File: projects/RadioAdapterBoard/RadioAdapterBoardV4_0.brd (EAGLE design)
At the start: 20.2 x 45.5 mm, 5 parts

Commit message: Added LTC3112 to Radio Adaptor Board
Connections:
- removed net N$2: R1.1
- net GND: now also R1.1
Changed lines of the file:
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@@
 <vertex x="-23" y="-1.25"/>
 </polygon>
-<wire x1="-8.57" y1="24.79" x2="-8.57" y2="25.79" width="0" layer="19" extent="1-1"/>
-<wire x1="-8.57" y1="24.29" x2="-8.57" y2="24.79" width="0" layer="19" extent="1-1"/>
-<wire x1="-8.57" y1="23.79" x2="-8.57" y2="24.29" width="0" layer="19" extent="1-1"/>
-<wire x1="-8.57" y1="21.29" x2="-8.57" y2="23.79" width="0" layer="19" extent="1-1"/>
+<contactref element="R1" pad="1"/>
+<wire x1="-13.27" y1="18.79" x2="-35.4" y2="-24.5" width="0" layer="19" extent="1-1"/>
+<wire x1="-13.27" y1="20.79" x2="-13.27" y2="18.79" width="0" layer="19" extent="1-1"/>
+<wire x1="-13.27" y1="21.29" x2="-13.27" y2="20.79" width="0" layer="19" extent="1-1"/>
+<wire x1="-8.57" y1="21.29" x2="-13.27" y2="21.29" width="0" layer="19" extent="1-1"/>
 <wire x1="-8.57" y1="20.79" x2="-8.57" y2="21.29" width="0" layer="19" extent="1-1"/>
+<wire x1="-8.57" y1="23.79" x2="-8.57" y2="21.29" width="0" layer="19" extent="1-1"/>
+<wire x1="-8.57" y1="24.29" x2="-8.57" y2="23.79" width="0" layer="19" extent="1-1"/>
+<wire x1="-8.57" y1="24.79" x2="-8.57" y2="24.29" width="0" layer="19" extent="1-1"/>
+<wire x1="-8.57" y1="25.79" x2="-8.57" y2="24.79" width="0" layer="19" extent="1-1"/>
 <wire x1="-4.8752" y1="21.841" x2="-8.57" y2="21.29" width="0" layer="19" extent="1-1"/>
 <wire x1="-2.8752" y1="21.841" x2="-4.8752" y2="21.841" width="0" layer="19" extent="1-1"/>
-<wire x1="-13.27" y1="21.29" x2="-8.57" y2="21.29" width="0" layer="19" extent="1-1"/>
-<wire x1="-13.27" y1="20.79" x2="-13.27" y2="21.29" width="0" layer="19" extent="1-1"/>
-<wire x1="-13.27" y1="18.79" x2="-13.27" y2="20.79" width="0" layer="19" extent="1-1"/>
 </signal>
 <signal name="3V6">
@@
 <wire x1="-29.8625" y1="-20.4" x2="-33.6" y2="-28.75" width="0" layer="19" extent="1-1"/>
 </signal>
-<signal name="N$2">
-<contactref element="R1" pad="1"/>
-</signal>
 </signals>

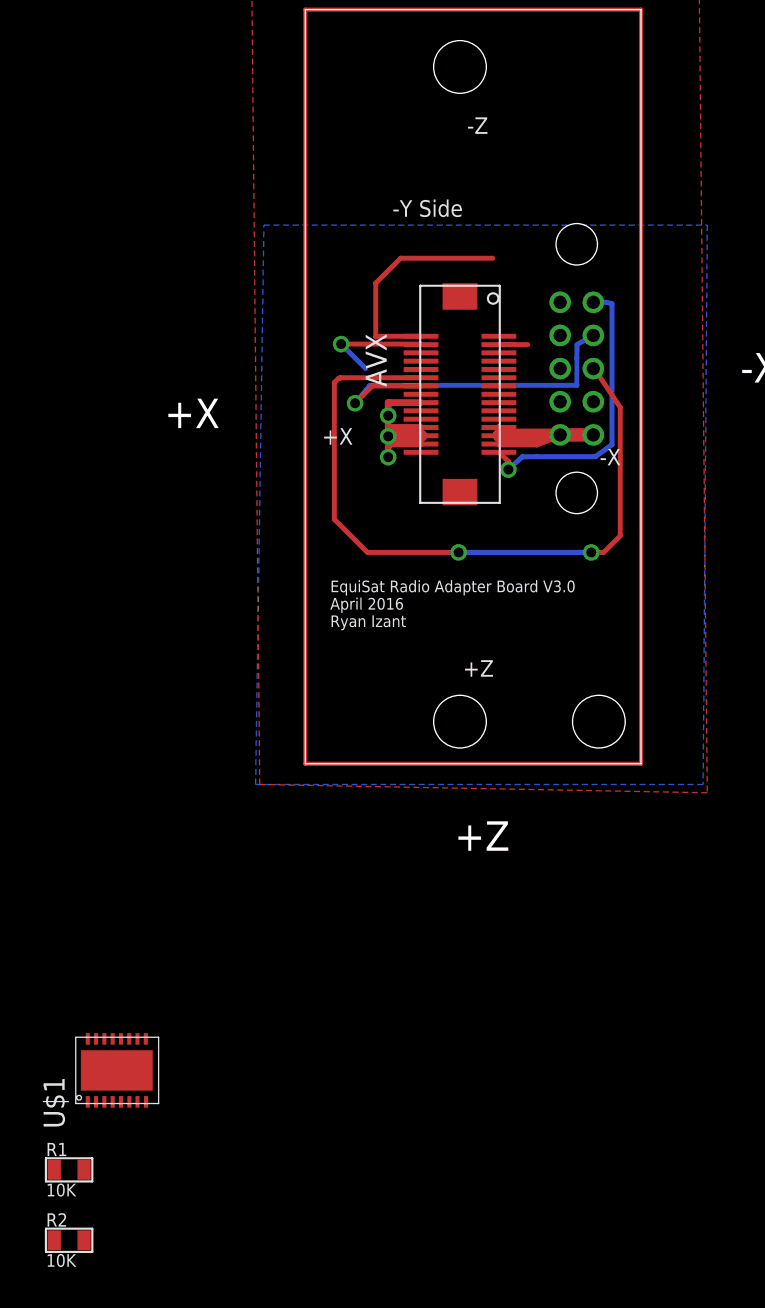
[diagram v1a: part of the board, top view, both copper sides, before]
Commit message: Changes to Radio Adapter Board V4
Moved LEDs to Radio Adapter Board
Flipped the connection to the radio so the radio is pointing into the
board
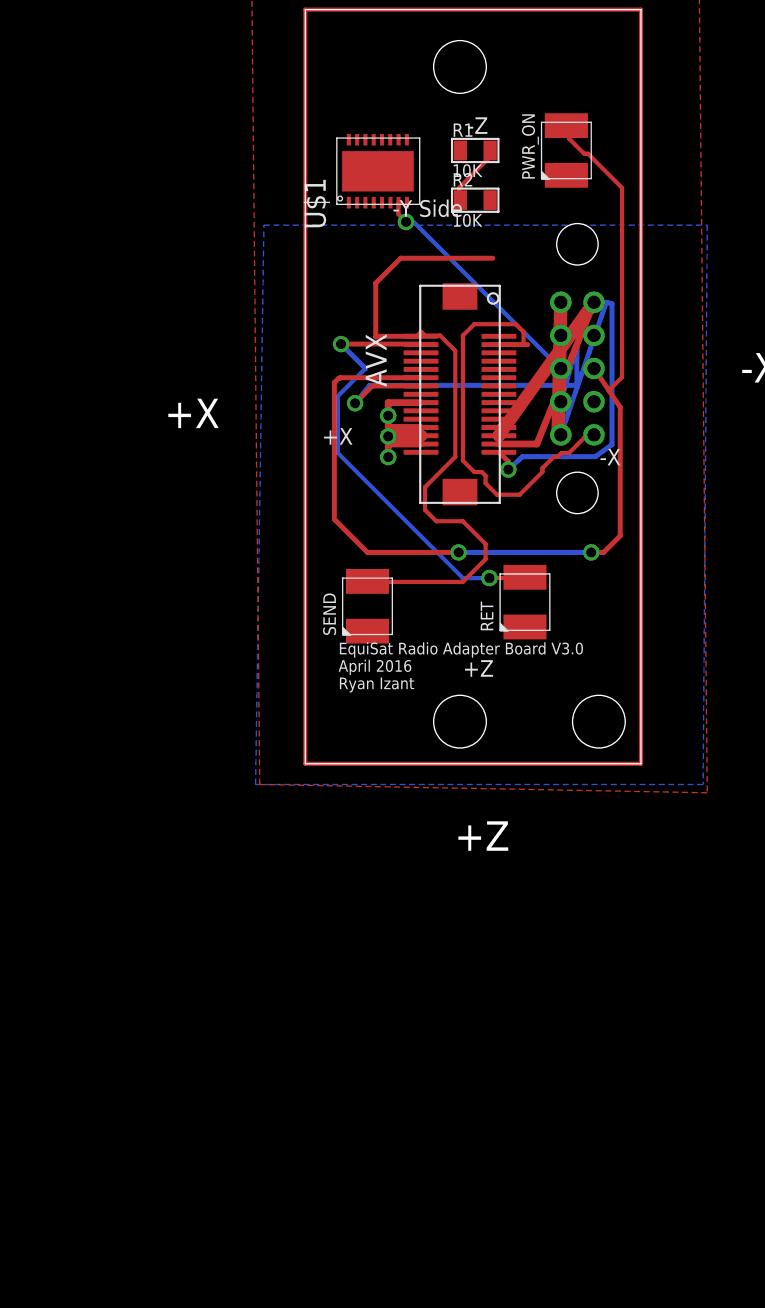
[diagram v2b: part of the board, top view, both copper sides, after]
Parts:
- added PWR_ON, RET, SEND: LT-T673-Q1R2-25-Z, CNTRL_BOARD:PLCC-2
- moved R2 67.4 mm to (-10.0, 34.0)
- moved R1 66.2 mm to (-10.0, 37.0)
- moved U$1 56.5 mm to (-17.8, 33.5)
- moved CNTRLCONN 8.25 mm to (-4.86, 27.8), turned to 270 degrees
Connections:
- net GND: now also PWR_ON.C, RET.C, SEND.C
- net P12: now also PWR_ON.A
- net P2: now also SEND.A
- net P4: now also RET.A
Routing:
- net P2: track 13.7 -> 40.2 mm
- net P3: track 1.74 -> 24.9 mm
- net P4: track 6.93 -> 27.2 mm, vias 1 -> 2
- net 3V6: track 20.4 -> 40.2 mm
- net P12: track 42.6 -> 60.4 mm
- net 3V6-SNS: track 0.00 -> 14.3 mm, vias 0 -> 1
- net P29: track 17.7 -> 25.4 mm
- net 3V6-REF: track 0.00 -> 3.96 mm
- net P14: track 21.9 -> 24.3 mm

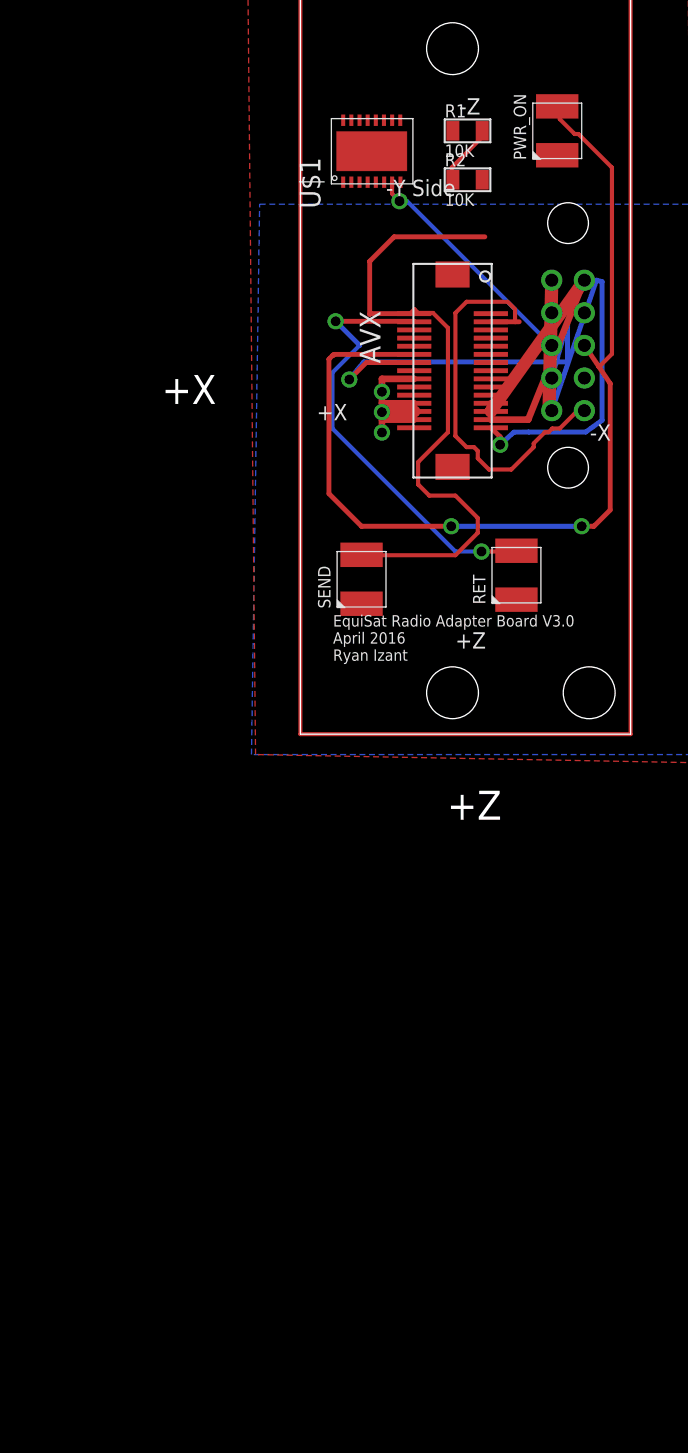
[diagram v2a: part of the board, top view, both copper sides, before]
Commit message: changes to Radio Adapter Board V4
Added the connections to LTC3112
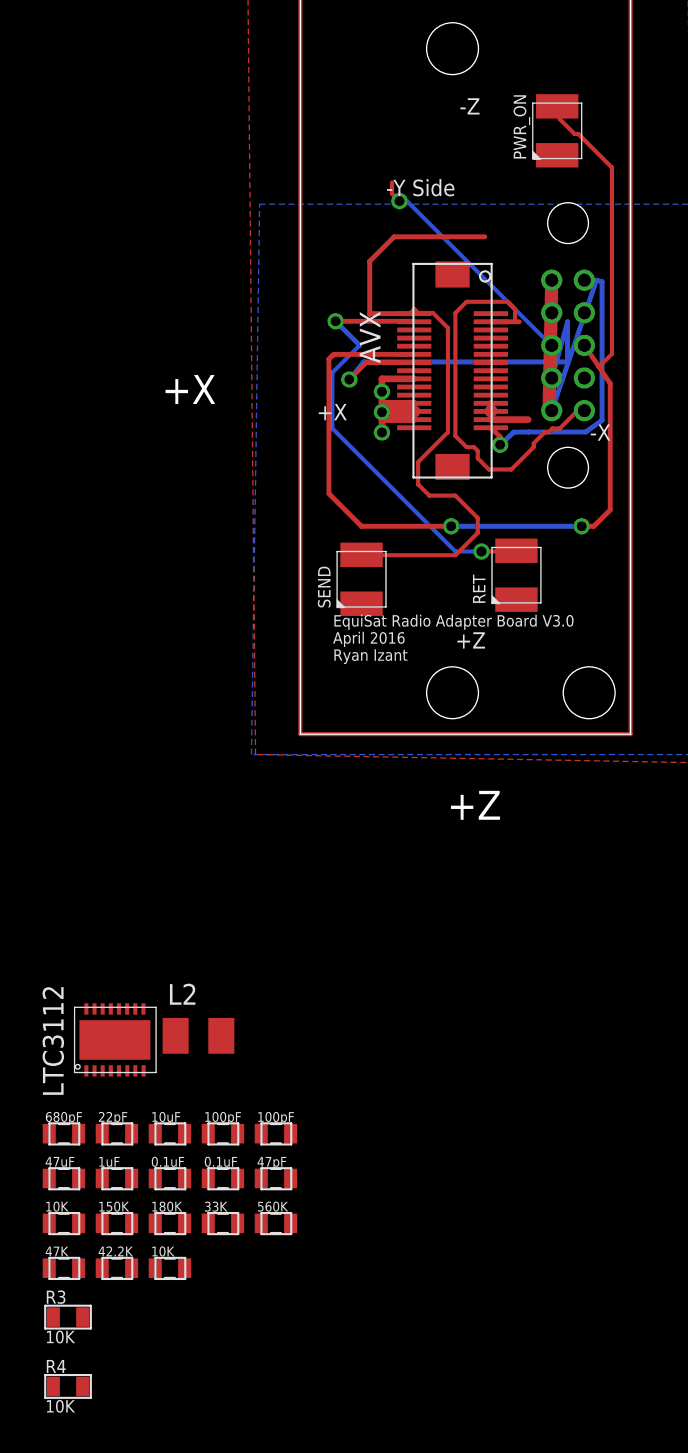
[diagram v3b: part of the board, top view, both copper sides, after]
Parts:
- removed R1, R2: 10K, BrownSpaceEngineering:0805
- removed U$1: (no value), CNTRL_BOARD:DHD16
- added C14: 680pF, CNTRL_BOARD:0805
- added C15: 22pF, CNTRL_BOARD:0805
- added C16: 10uF, CNTRL_BOARD:0805
- added C17, C18: 100pF, CNTRL_BOARD:0805
- added C19: 47uF, CNTRL_BOARD:0805
- added C20: 1uF, CNTRL_BOARD:0805
- added C21, C22: 0.1uF, CNTRL_BOARD:0805
- added C23: 47pF, CNTRL_BOARD:0805
- added L2: 4.7uH, resistor:L3225M
- added LTC3112: (no value), CNTRL_BOARD:DHD16
- added R10: 47K, CNTRL_BOARD:0805
- added R11: 42.2K, CNTRL_BOARD:0805
- added R12, R5: 10K, CNTRL_BOARD:0805
- added R3, R4: 10K, BrownSpaceEngineering:0805
- added R6: 150K, CNTRL_BOARD:0805
- added R7: 180K, CNTRL_BOARD:0805
- added R8: 33K, CNTRL_BOARD:0805
- added R9: 560K, CNTRL_BOARD:0805
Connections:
- removed net N$3: R2.2, U$1.8
- new net COMP: C14.2, C15.1, LTC3112.1
- new net FB: C15.2, LTC3112.2, R12.1, R6.1, R8.2, R9.2
- new net N$23: C20.2, LTC3112.15
- new net N$25: C22.1, LTC3112.14
- new net N$26: C22.2, L2.2, LTC3112.12, LTC3112.13
- new net N$28: C21.2, L2.1, LTC3112.10, LTC3112.9
- new net N$29: C21.1, LTC3112.11
- new net N$4: C14.1, R8.1
- new net N$5: C23.2, R12.2
- new net N$6: R5.1, R6.2
- new net OVP: C17.1, LTC3112.3, R10.2, R7.1
- new net VIN: C16.1, CNTRLCONN.P$1, CNTRLCONN.P$10, LTC3112.16, LTC3112.4, LTC3112.5
- net 3V6: now also C19.1, C23.1, LTC3112.8, R4.2, R7.2, R9.1; no longer CNTRLCONN.P$1, CNTRLCONN.P$10
- net 3V6-EN: now also LTC3112.6; no longer U$1.6
- net 3V6-REF: now also R3.2, R4.1; no longer R1.2, R2.1
- net 3V6-SNS: now also C18.1, LTC3112.7, R11.2; no longer U$1.7
- net GND: now also C16.2, C17.2, C18.2, C19.2, C20.1, LTC3112.17, R10.1, R11.1, R3.1, R5.2; no longer R1.1
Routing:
- net 3V6: track 40.2 -> 13.0 mm
- net VIN: track 0.00 -> 8.09 mm
- net 3V6-REF: track 3.96 -> 0.00 mm

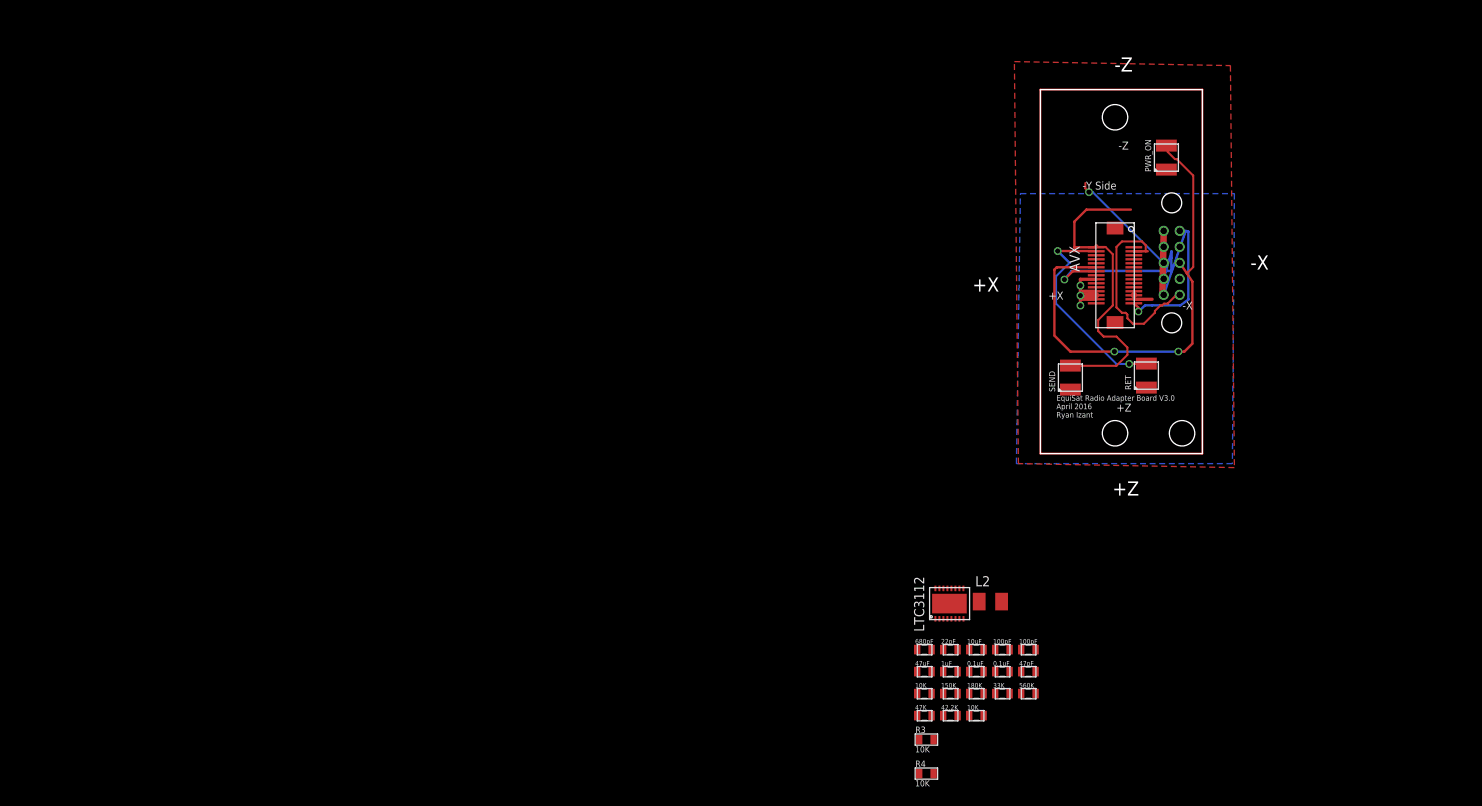
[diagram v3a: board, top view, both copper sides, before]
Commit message: Changes to Radio Adapter Board v4
In process of reordering physical components.
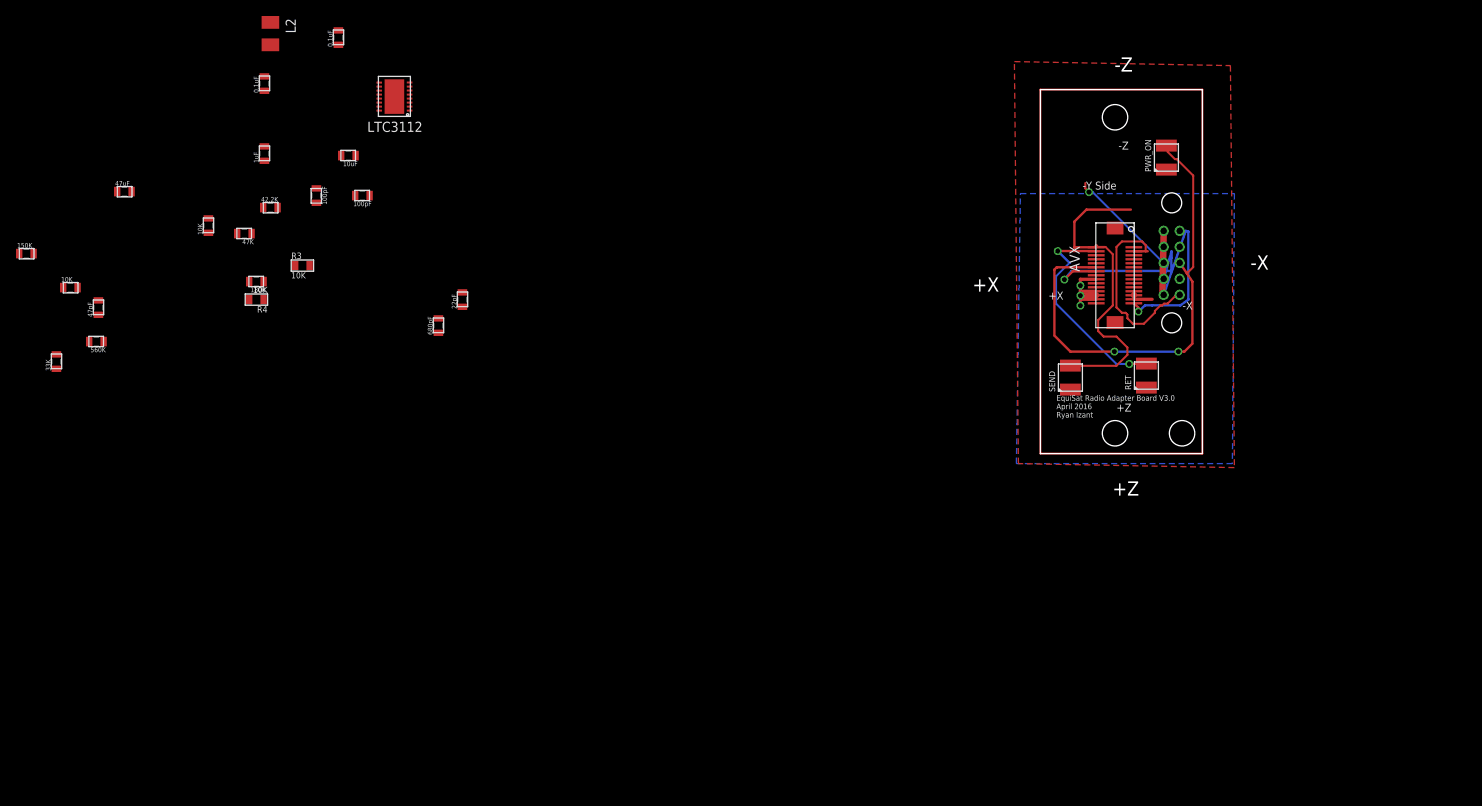
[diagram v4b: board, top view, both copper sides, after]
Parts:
- moved R6 127.9 mm to (-147.0, 25.0)
- moved R8 125.3 mm to (-143.2, 11.5), turned to 90 degrees
- moved R12 125.3 mm to (-141.5, 20.8)
- moved C23 124.8 mm to (-138.0, 18.2), turned to 90 degrees
- moved R9 124.5 mm to (-138.2, 14.0), turned to 180 degrees
- moved C22 118.0 mm to (-117.2, 46.2), turned to 90 degrees
- moved C19 116.6 mm to (-134.8, 32.8)
- moved L2 114.6 mm to (-116.5, 52.5), turned to 270 degrees
- moved C21 112.4 mm to (-108.0, 52.0), turned to 90 degrees
- moved C20 107.5 mm to (-117.2, 37.5), turned to 90 degrees
- moved R5 106.9 mm to (-124.2, 28.5), turned to 90 degrees
- moved R11 106.1 mm to (-116.5, 30.8)
- moved C18 105.6 mm to (-110.8, 32.2), turned to 270 degrees
- moved R10 104.2 mm to (-119.8, 27.5), turned to 180 degrees
- moved R7 103.7 mm to (-118.2, 21.5), turned to 180 degrees
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
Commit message: Changes to Radio Adapter Board
In Process of Optimizing the Physical Layout
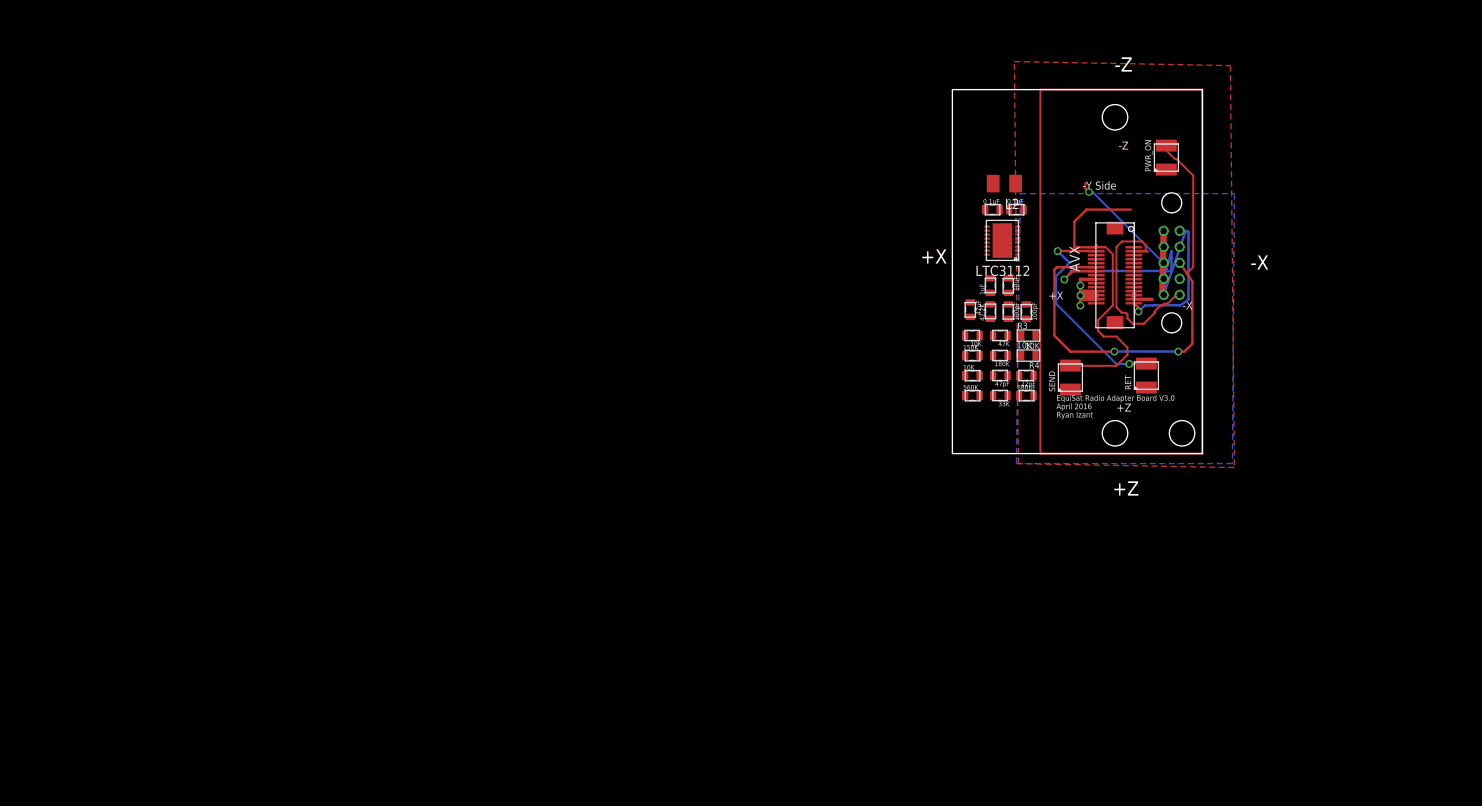
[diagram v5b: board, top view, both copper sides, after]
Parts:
- moved R6 118.9 mm to (-28.8, 12.2)
- moved R8 118.1 mm to (-25.2, 7.25), turned to 180 degrees
- moved R12 113.3 mm to (-28.8, 9.75)
- moved C23 113.1 mm to (-25.2, 9.75), turned to 180 degrees
- moved R9 109.7 mm to (-28.8, 7.25), turned to 0 degrees
- moved C19 106.8 mm to (-29.0, 18.0), turned to 270 degrees
- moved R4 96.8 mm to (-21.8, 12.2)
- moved R5 96.5 mm to (-28.8, 14.8), turned to 180 degrees
- moved R10 95.4 mm to (-25.2, 14.8)
- moved L2 93.6 mm to (-24.8, 33.8), turned to 180 degrees
- moved R7 93.5 mm to (-25.2, 12.2)
- moved C22 92.4 mm to (-26.2, 30.5), turned to 0 degrees
- moved C20 92.2 mm to (-26.5, 21.0)
- moved R3 91.2 mm to (-21.8, 14.8)
- moved R11 90.9 mm to (-26.5, 17.8), turned to 90 degrees
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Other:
- board size 20.2 x 45.5 mm -> 31.2 x 45.5 mm
